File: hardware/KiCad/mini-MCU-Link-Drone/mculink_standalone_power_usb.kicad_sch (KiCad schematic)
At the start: 39 parts, among them J1 USB4110-GF-A_REVB, U1 XC6227C331PR-G, U2 LPC55S69JBD64, Y1 16.000MHz

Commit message: updated schematic part
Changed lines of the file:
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@@
     (company "Lucerne University of Applied Sciences and Arts")
   )
+  (junction (at 46.99 138.43) (diameter 0) (color 0 0 0 0)
+  )
   (junction (at 86.36 138.43) (diameter 0) (color 0 0 0 0)
   )
@@
   (junction (at 179.07 38.1) (diameter 0) (color 0 0 0 0)
   )
+  (junction (at 171.45 35.56) (diameter 0) (color 0 0 0 0)
+  )
   (junction (at 87.63 86.36) (diameter 0) (color 0 0 0 0)
   )
@@
   (junction (at 166.37 86.36) (diameter 0) (color 0 0 0 0)
   )
+  (junction (at 27.94 176.53) (diameter 0) (color 0 0 0 0)
+  )
   (junction (at 179.07 35.56) (diameter 0) (color 0 0 0 0)
   )
@@
   (junction (at 260.35 82.55) (diameter 0) (color 0 0 0 0)
   )
+  (junction (at 34.29 86.36) (diameter 0) (color 0 0 0 0)
+  )
   (junction (at 39.37 149.86) (diameter 0) (color 0 0 0 0)
   )
@@
     (stroke (width 0) (type default))
   )
-  (wire (pts (xy 39.37 138.43) (xy 69.85 138.43))
+  (wire (pts (xy 39.37 138.43) (xy 46.99 138.43))
     (stroke (width 0) (type default))
   )
@@
     (stroke (width 0) (type default))
   )
-  (wire (pts (xy 154.94 35.56) (xy 179.07 35.56))
+  (wire (pts (xy 154.94 35.56) (xy 171.45 35.56))
     (stroke (width 0) (type default))
   )
@@
     (stroke (width 0) (type default))
   )
+  (wire (pts (xy 171.45 35.56) (xy 179.07 35.56))
+    (stroke (width 0) (type default))
+  )
   (wire (pts (xy 217.17 90.17) (xy 219.71 90.17))
     (stroke (width 0) (type default))
@@
     (stroke (width 0) (type default))
   )
+  (wire (pts (xy 34.29 86.36) (xy 26.67 86.36))
+    (stroke (width 0) (type default))
+  )
   (wire (pts (xy 154.94 66.04) (xy 154.94 67.31))
     (stroke (width 0) (type default))
@@
     (stroke (width 0) (type default))
   )
+  (wire (pts (xy 46.99 138.43) (xy 69.85 138.43))
+    (stroke (width 0) (type default))
+  )
   (wire (pts (xy 146.05 139.7) (xy 143.51 139.7))
     (stroke (width 0) (type default))
@@
     (stroke (width 0) (type default))
   )
-  (wire (pts (xy 39.37 86.36) (xy 26.67 86.36))
+  (wire (pts (xy 39.37 86.36) (xy 34.29 86.36))
     (stroke (width 0) (type default))
   )
@@
     )
   )
+  (symbol (lib_id "power:PWR_FLAG") (at 46.99 138.43 0) (unit 1)
+    (in_bom yes) (on_board yes) (dnp no) (fields_autoplaced)
+    (property "Reference" "#FLG01" (at 46.99 136.525 0)
+      (effects (font (size 1.27 1.27)) hide)
+    )
+    (property "Value" "PWR_FLAG" (at 46.99 134.2969 0)
+      (effects (font (size 1.27 1.27)))
+    )
+    (property "Footprint" "" (at 46.99 138.43 0)
+      (effects (font (size 1.27 1.27)) hide)
+    )
+    (property "Datasheet" "~" (at 46.99 138.43 0)
+      (effects (font (size 1.27 1.27)) hide)
+    )
+    (pin "1")
+    (instances
+      (project "MCU-Link-Drone"
+        (path "/52afa5f9-012e-424b-bf0c-786f4ecc122a/ba3457e3-4ca3-42ff-b102-c41c2fbeeb1c"
+          (reference "#FLG01") (unit 1)
+        )
+      )
+    )
+  )
   (symbol (lib_id "power:GND") (at 154.94 67.31 0) (unit 1)
     (in_bom yes) (on_board yes) (dnp no)
@@
     )
   )
+  (symbol (lib_id "power:PWR_FLAG") (at 34.29 86.36 0) (unit 1)
+    (in_bom yes) (on_board yes) (dnp no) (fields_autoplaced)
+    (property "Reference" "#FLG03" (at 34.29 84.455 0)
+      (effects (font (size 1.27 1.27)) hide)
+    )
+    (property "Value" "PWR_FLAG" (at 34.29 82.2269 0)
+      (effects (font (size 1.27 1.27)))
+    )
+    (property "Footprint" "" (at 34.29 86.36 0)
+      (effects (font (size 1.27 1.27)) hide)
+    )
+    (property "Datasheet" "~" (at 34.29 86.36 0)
+      (effects (font (size 1.27 1.27)) hide)
+    )
+    (pin "1")
+    (instances
+      (project "MCU-Link-Drone"
+        (path "/52afa5f9-012e-424b-bf0c-786f4ecc122a/ba3457e3-4ca3-42ff-b102-c41c2fbeeb1c"
+          (reference "#FLG03") (unit 1)
+        )
+      )
+    )
+  )
   (symbol (lib_id "power:GND") (at 121.92 44.45 0) (unit 1)
     (in_bom yes) (on_board yes) (dnp no)
@@
     )
   )
+  (symbol (lib_id "power:PWR_FLAG") (at 27.94 176.53 270) (unit 1)
+    (in_bom yes) (on_board yes) (dnp no) (fields_autoplaced)
+    (property "Reference" "#FLG02" (at 29.845 176.53 0)
+      (effects (font (size 1.27 1.27)) hide)
+    )
+    (property "Value" "PWR_FLAG" (at 31.115 176.53 90)
+      (effects (font (size 1.27 1.27)) (justify left))
+    )
+    (property "Footprint" "" (at 27.94 176.53 0)
+      (effects (font (size 1.27 1.27)) hide)
+    )
+    (property "Datasheet" "~" (at 27.94 176.53 0)
+      (effects (font (size 1.27 1.27)) hide)
+    )
+    (pin "1")
+    (instances
+      (project "MCU-Link-Drone"
+        (path "/52afa5f9-012e-424b-bf0c-786f4ecc122a/ba3457e3-4ca3-42ff-b102-c41c2fbeeb1c"
+          (reference "#FLG02") (unit 1)
+        )
+      )
+    )
+  )
   (symbol (lib_id "Device:C") (at 256.54 49.53 0) (unit 1)
     (in_bom yes) (on_board yes) (dnp no)
@@
         )
       )
+    )
+  )
+  (symbol (lib_id "power:PWR_FLAG") (at 171.45 35.56 0) (unit 1)
+    (in_bom yes) (on_board yes) (dnp no) (fields_autoplaced)
+    (property "Reference" "#FLG04" (at 171.45 33.655 0)
+      (effects (font (size 1.27 1.27)) hide)
+    )
+    (property "Value" "PWR_FLAG" (at 171.45 31.4269 0)
+      (effects (font (size 1.27 1.27)))
+    )
+    (property "Footprint" "" (at 171.45 35.56 0)
+      (effects (font (size 1.27 1.27)) hide)
+    )
+    (property "Datasheet" "~" (at 171.45 35.56 0)
+      (effects (font (size 1.27 1.27)) hide)
+    )
+    (pin "1")
+    (instances
+      (project "MCU-Link-Drone"
+        (path "/52afa5f9-012e-424b-bf0c-786f4ecc122a/ba3457e3-4ca3-42ff-b102-c41c2fbeeb1c"
+          (reference "#FLG04") (unit 1)
+        )
+      )

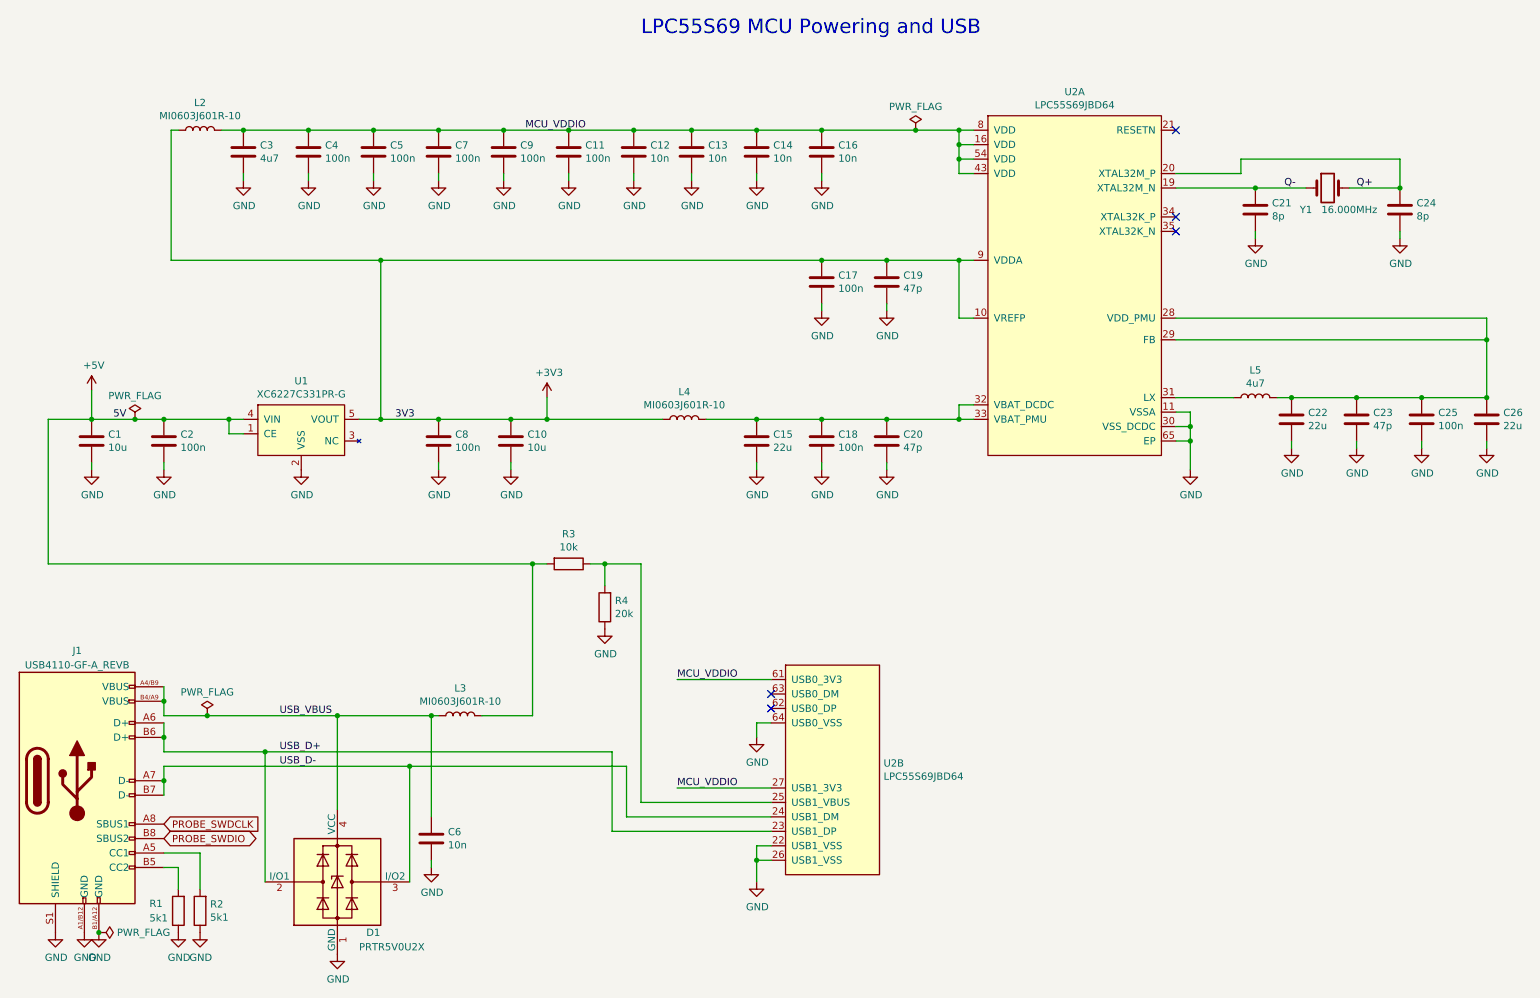
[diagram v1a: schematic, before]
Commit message: cleanup and ERC fixes
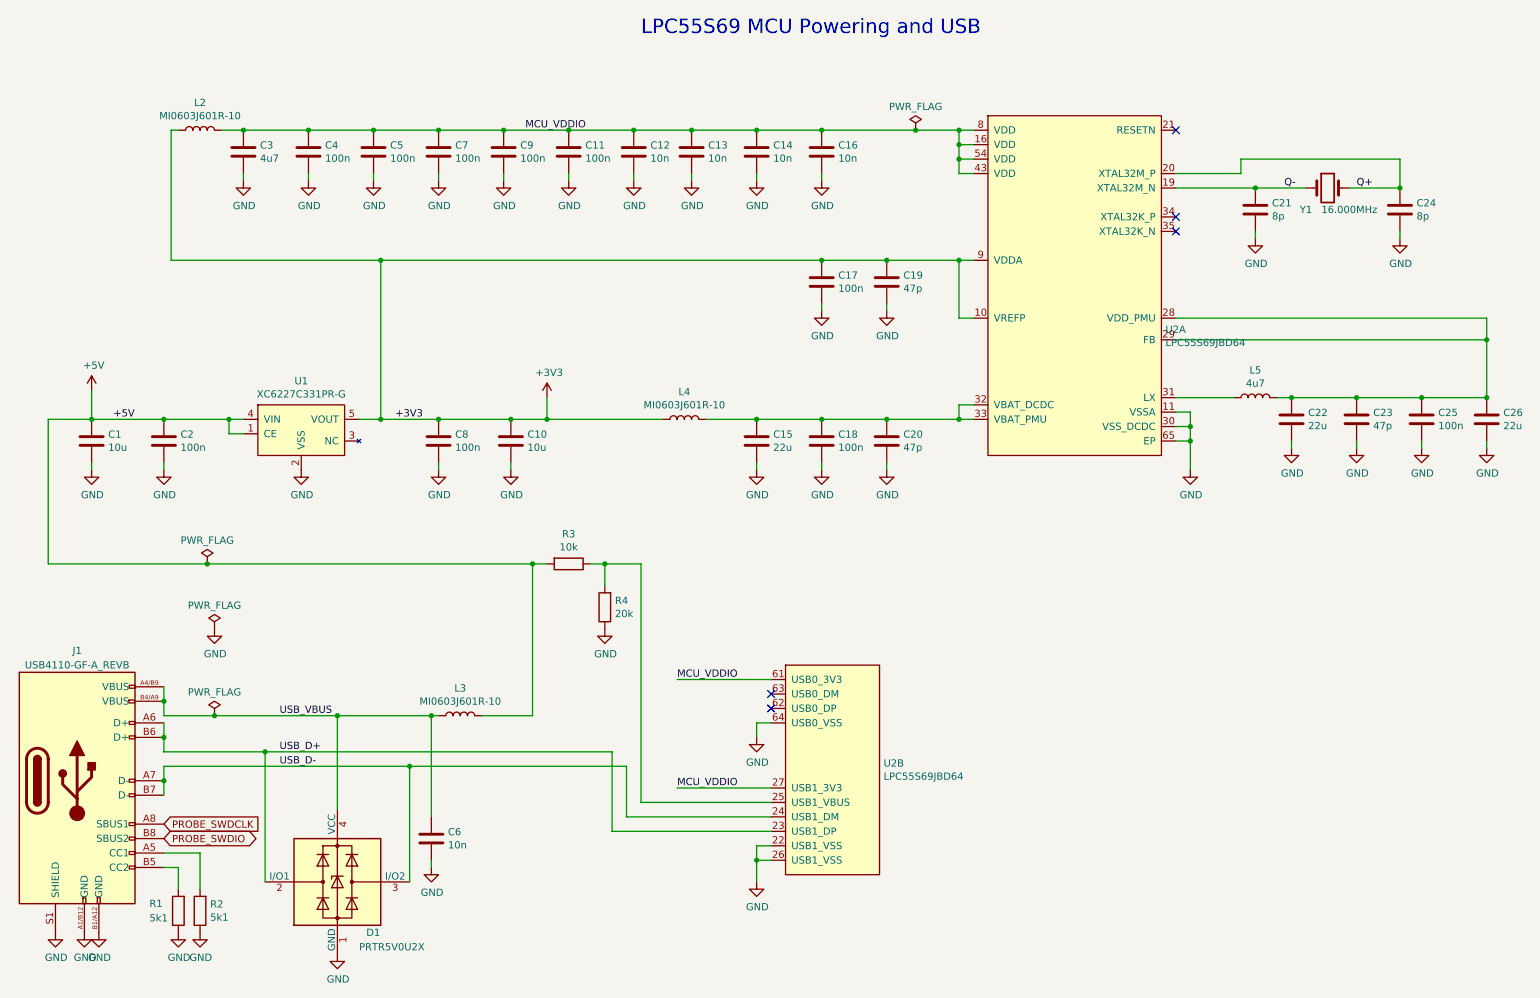
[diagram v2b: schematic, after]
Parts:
- D1: footprint mculink:SOT143B -> Package_TO_SOT_SMD:SOT-143
- J1: footprint mculink:USB_C_Receptacle_GCT_USB4110-GF-A -> mculink:GCT_USB4110-GF-A_REVB
- U1: symbol mculink_kicad:XC6227C331PR-G -> mcuoneclipse:XC6227C331PR-G
- U2: symbol mculink_kicad:LPC55S69JBD64 -> mcuoneclipse:LPC55S69JBD64_USB
- U2: symbol mculink_kicad:LPC55S69JBD64 -> mcuoneclipse:LPC55S69JBD64_Power

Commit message: made it warning free with KiCAD 8
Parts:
- U2: symbol mcuoneclipse:LPC55S69JBD64_USB -> mcuoneclipse:LPC55S69JBD64
- U2: symbol mcuoneclipse:LPC55S69JBD64_Power -> mcuoneclipse:LPC55S69JBD64
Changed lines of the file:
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@@
 	)
 	(symbol
-		(lib_id "mcuoneclipse:LPC55S69JBD64_USB")
+		(lib_id "mcuoneclipse:LPC55S69JBD64")
 		(at 148.59 147.32 0)
 		(unit 2)
@@
 	)
 	(symbol
-		(lib_id "mcuoneclipse:LPC55S69JBD64_Power")
+		(lib_id "mcuoneclipse:LPC55S69JBD64")
 		(at 198.12 71.12 0)
 		(unit 1)
